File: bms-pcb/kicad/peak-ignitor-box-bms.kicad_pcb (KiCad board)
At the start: 4 copper layers, 85 x 99 mm, 5 parts, among them J1 Conn_01x02, J2 Conn_01x05, J3 Conn_01x01, J4 Conn_01x01, U1 BMS-4s-40A

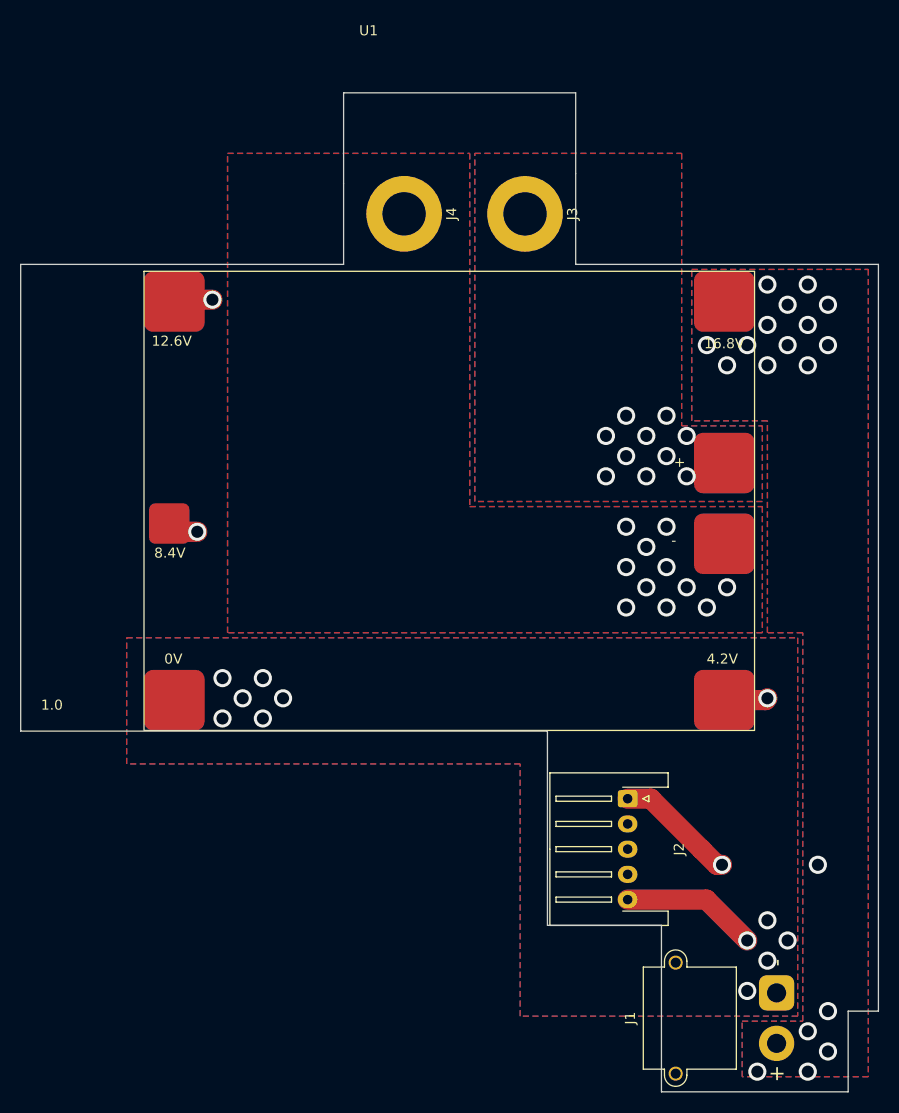
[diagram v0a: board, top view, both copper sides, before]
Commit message: updated bms carrier
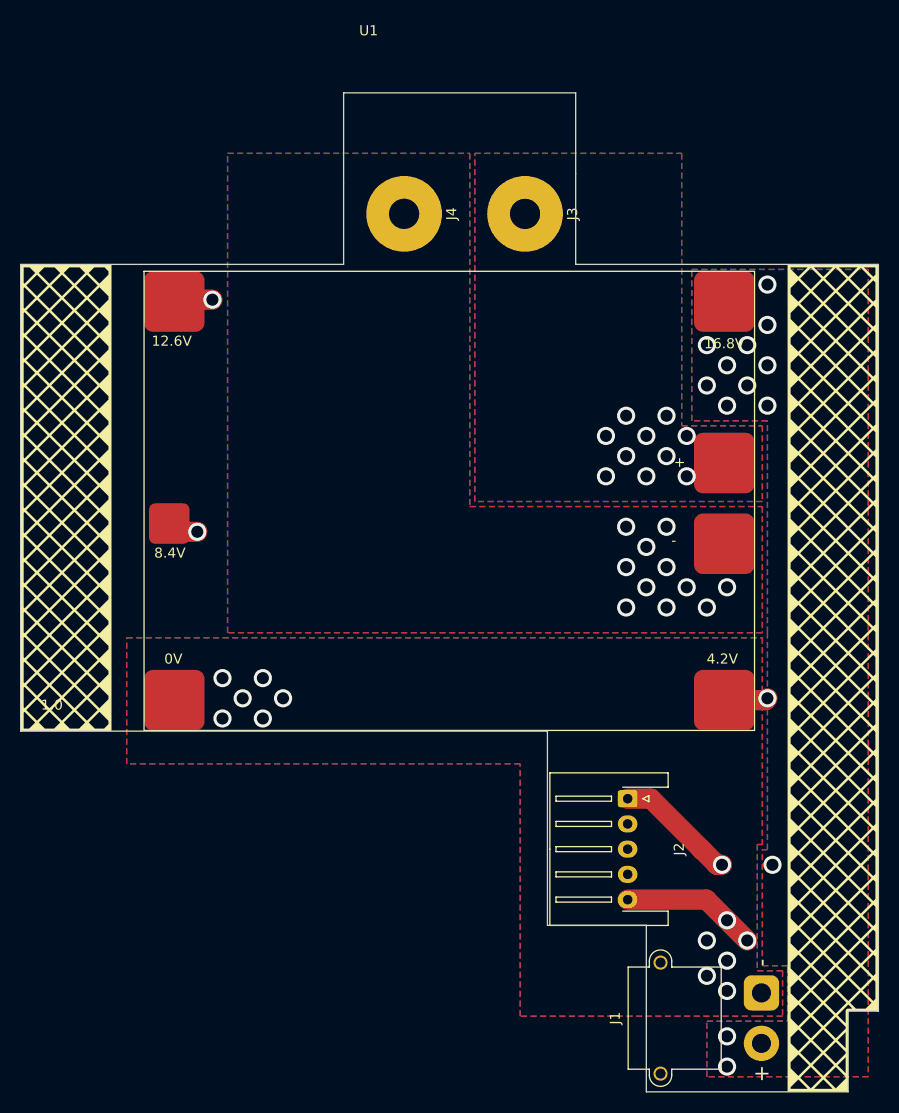
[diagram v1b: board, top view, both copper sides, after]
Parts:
- moved J1 1.50 mm to (151.4, 105.2)
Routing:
- net Net-(J1-Pin_2): track 21.6 -> 17.1 mm, vias 20 -> 14
- net Net-(J1-Pin_1): vias 11 -> 12
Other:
- outline, holes or cut-outs redrawn
